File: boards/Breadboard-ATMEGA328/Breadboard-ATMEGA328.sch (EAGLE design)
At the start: 10 parts, among them IC1 ATMEGA328P-PU, J1 PINHD-1X7, J2 PINHD-1X7, J3 PINHD-1X7, J4 PINHD-1X7

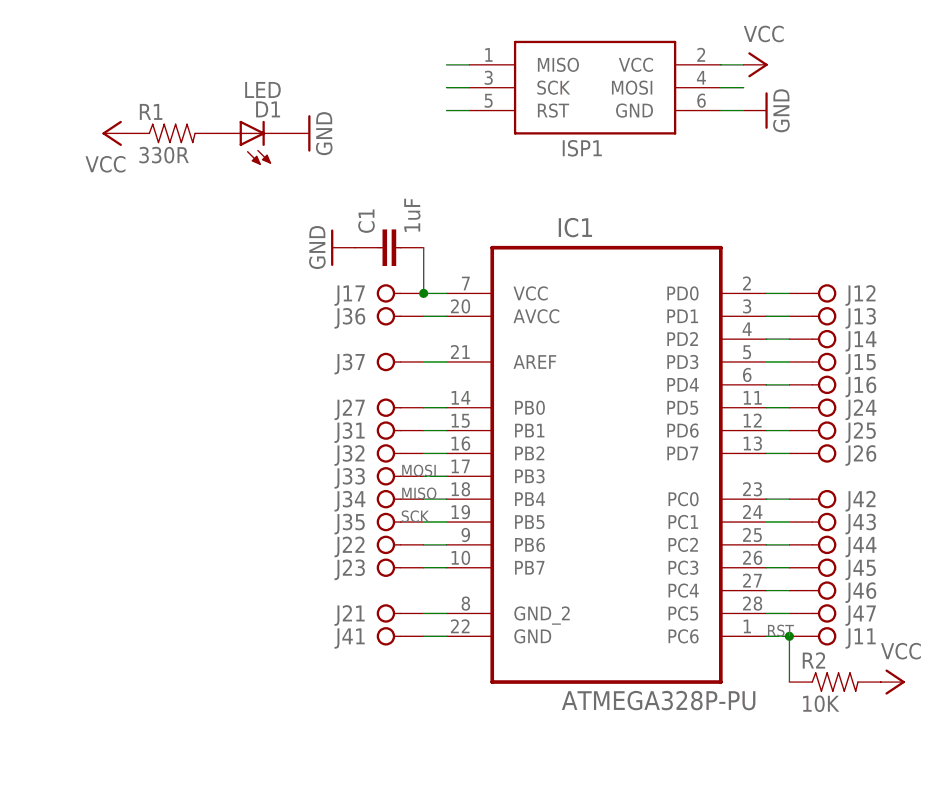
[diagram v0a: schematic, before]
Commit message: Updated breadboard ATMega328
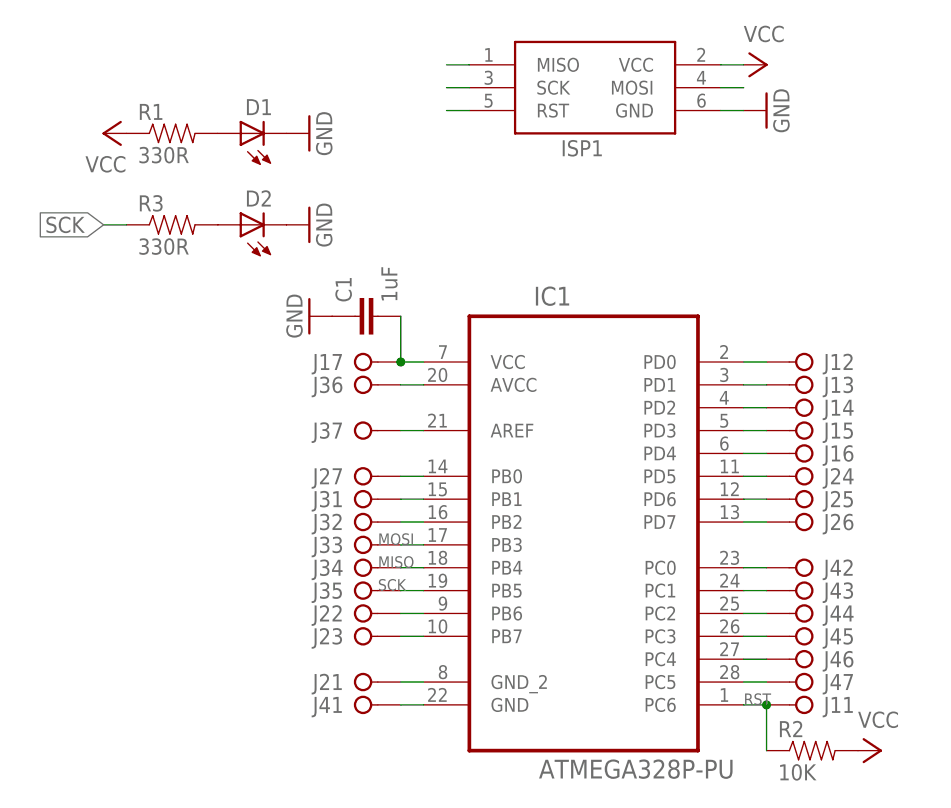
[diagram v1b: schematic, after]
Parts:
- added D2: LED-0805, SaintGimp:LED-0805
- added R3: 330R, SaintGimp:RESISTOR-0805
- D1: value LED -> LED-0805; device SaintGimp:LED -> SaintGimp:LED-0805
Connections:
- new net N$8: D2.A, R3.2
- net GND: now also D2.C
- net SCK: now also R3.1
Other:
- moved on the sheet: C1, IC1, J11, J12, J13, J14, J15, J16, J17, J21, J22, J23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
